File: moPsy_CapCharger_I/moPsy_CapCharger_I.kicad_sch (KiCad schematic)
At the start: 11 parts, among them J1 Conn_01x08_Male, U1 LM79L12_TO92, U2 LM555xN

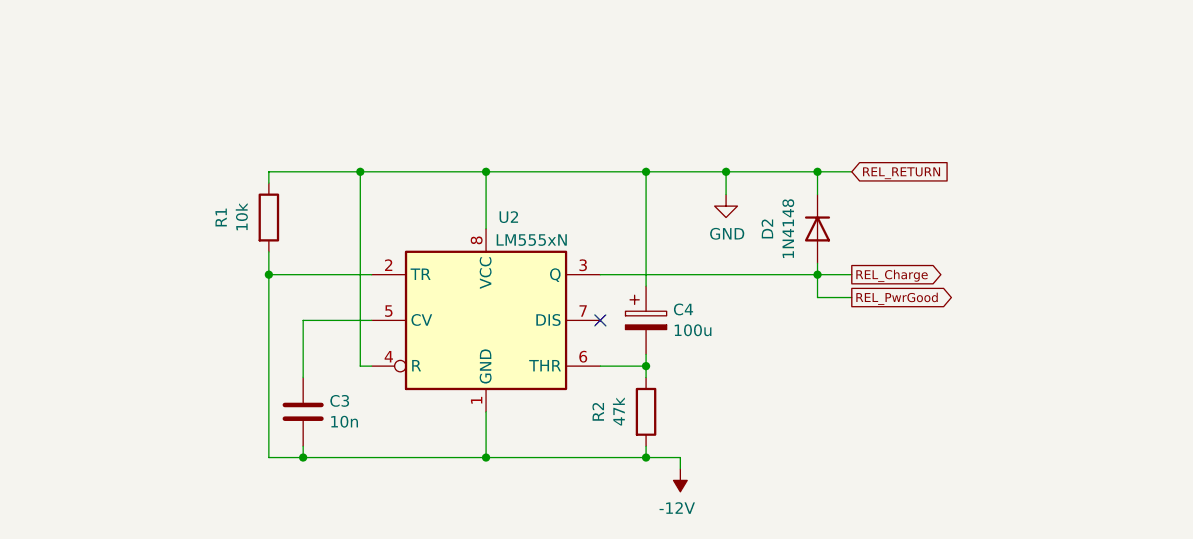
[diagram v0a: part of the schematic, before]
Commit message: Fix the Cap Charger circuit
The previous circuit did the wrong thing. This one is based
on https://elektro.turanis.de/html/prj248/index.html and has
the correct behaviour.

In the end, an RC element and a trigger are needed.
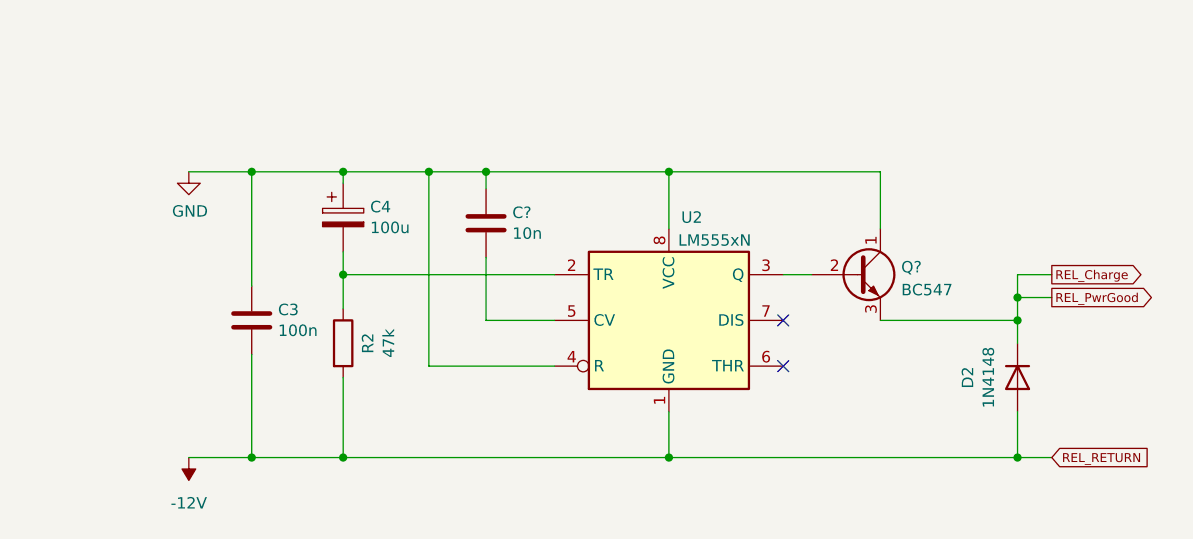
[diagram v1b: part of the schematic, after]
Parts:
- removed R1: 10k, Resistor_THT:R_Axial_DIN0207_L6.3mm_D2.5mm_P7.62mm_Horizontal, symbol Device:R
- added C?: 10n, Capacitor_THT:C_Rect_L7.0mm_W2.5mm_P5.00mm, symbol Device:C
- added Q?: BC547, Package_TO_SOT_THT:TO-92_Inline, symbol Transistor_BJT:BC547
- C2: footprint Capacitor_THT:CP_Radial_D8.0mm_P3.50mm -> Capacitor_THT:C_Rect_L7.0mm_W2.5mm_P5.00mm
- C3: value 10n -> 100n
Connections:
- net -12V: now also D2.2 (A), J1.8 (Pin_8); no longer U2.2 (TR)
- net GND: now also C3.1, C?.1, Q?.1 (C); no longer D2.1 (K), J1.8 (Pin_8)
- net REL_Charge: now also D2.1 (K), Q?.3 (E); no longer D2.2 (A), U2.3 (Q)
- net at U2.5 (CV): now also C?.2; no longer C3.1
- net at C4.2, R2.1: now also U2.2 (TR); no longer U2.6 (THR)
- new net: Q?.2 (B), U2.3 (Q)
- no-connect marks 1 -> 2
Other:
- moved on the sheet: C3, C4, D2, R2, U2

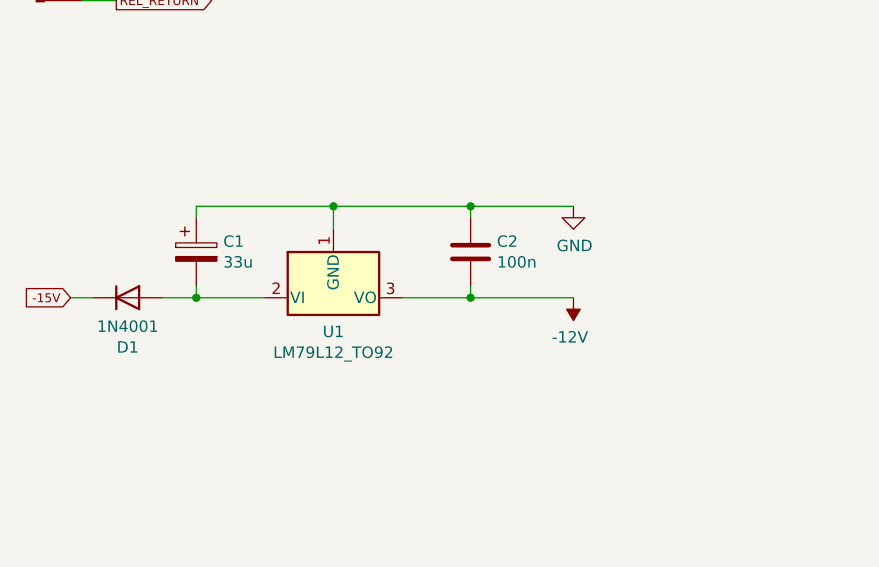
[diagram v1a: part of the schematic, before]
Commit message: Add a charge capacitor
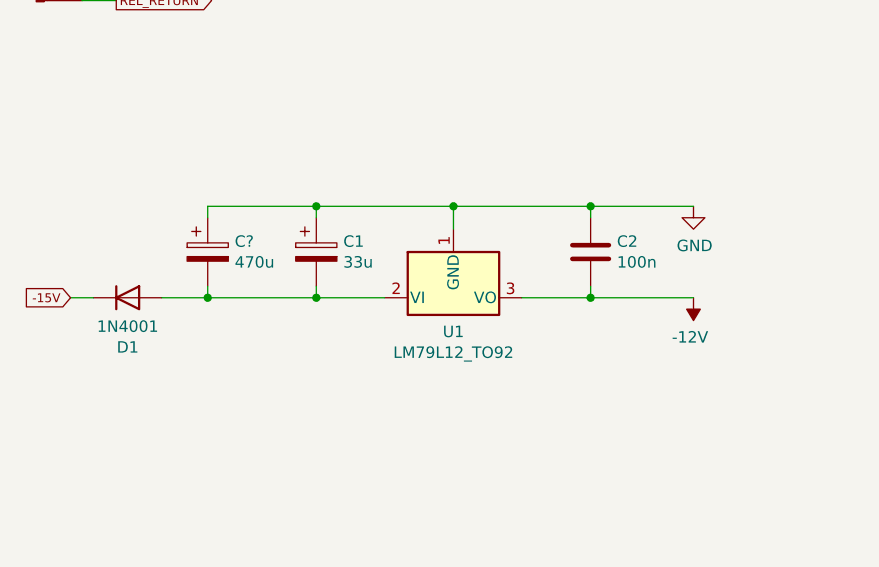
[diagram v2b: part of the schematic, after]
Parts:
- added C?: 470u, Capacitor_THT:CP_Radial_D8.0mm_P3.50mm, symbol Device:CP
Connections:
- net GND: now also C?.1
- net at C1.2, D1.2 (A), U1.2 (VI): now also C?.2
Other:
- moved on the sheet: C1, C2, U1

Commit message: Design a new PCB for the cap charger
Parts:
- C1: renamed from C?; footprint Capacitor_THT:CP_Radial_D8.0mm_P3.50mm -> Capacitor_THT:C_Axial_L19.0mm_D9.5mm_P25.00mm_Horizontal
- C4: renamed from C3; Reichelt (none) -> COS 105 470/16
- gave numbers to parts that had none: 2
- renumbered C1 to C2, C2 to C3, C4 to C5, R2 to R1
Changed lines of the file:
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@@
   (symbol (lib_id "Device:CP") (at 52.705 67.31 0) (unit 1)
     (in_bom yes) (on_board yes)
-    (property "Reference" "C1" (id 0) (at 55.7022 66.1416 0)
+    (property "Reference" "C2" (id 0) (at 55.7022 66.1416 0)
       (effects (font (size 1.27 1.27)) (justify left))
     )
@@
   (symbol (lib_id "Device:C") (at 83.185 67.31 0) (unit 1)
     (in_bom yes) (on_board yes)
-    (property "Reference" "C2" (id 0) (at 86.106 66.1416 0)
+    (property "Reference" "C3" (id 0) (at 86.106 66.1416 0)
       (effects (font (size 1.27 1.27)) (justify left))
     )
@@
   (symbol (lib_id "power:-12V") (at 94.615 72.39 180) (unit 1)
     (in_bom yes) (on_board yes)
-    (property "Reference" "#PWR0104" (id 0) (at 94.615 74.93 0)
+    (property "Reference" "#PWR03" (id 0) (at 94.615 74.93 0)
       (effects (font (size 1.27 1.27)) hide)
     )
@@
   (symbol (lib_id "power:GND") (at 94.615 62.23 0) (unit 1)
     (in_bom yes) (on_board yes)
-    (property "Reference" "#PWR0103" (id 0) (at 94.615 68.58 0)
+    (property "Reference" "#PWR02" (id 0) (at 94.615 68.58 0)
       (effects (font (size 1.27 1.27)) hide)
     )
@@
   (symbol (lib_id "Device:CP") (at 141.605 81.28 0) (unit 1)
     (in_bom yes) (on_board yes)
-    (property "Reference" "C4" (id 0) (at 144.6022 80.1116 0)
+    (property "Reference" "C5" (id 0) (at 144.6022 80.1116 0)
       (effects (font (size 1.27 1.27)) (justify left))
     )
@@
   (symbol (lib_id "Device:R") (at 141.605 95.25 0) (unit 1)
     (in_bom yes) (on_board yes)
-    (property "Reference" "R2" (id 0) (at 144.3736 95.25 90))
+    (property "Reference" "R1" (id 0) (at 144.3736 95.25 90))
     (property "Value" "47k" (id 1) (at 146.685 95.25 90))
     (property "Footprint" "Resistor_THT:R_Axial_DIN0207_L6.3mm_D2.5mm_P7.62mm_Horizontal" (id 2) (at 139.827 95.25 90)
@@
   (symbol (lib_id "power:-12V") (at 124.46 107.95 180) (unit 1)
     (in_bom yes) (on_board yes)
-    (property "Reference" "#PWR0101" (id 0) (at 124.46 110.49 0)
+    (property "Reference" "#PWR05" (id 0) (at 124.46 110.49 0)
       (effects (font (size 1.27 1.27)) hide)
     )
@@
   (symbol (lib_id "power:GND") (at 124.46 76.2 0) (unit 1)
     (in_bom yes) (on_board yes)
-    (property "Reference" "#PWR0102" (id 0) (at 124.46 82.55 0)
+    (property "Reference" "#PWR04" (id 0) (at 124.46 82.55 0)
       (effects (font (size 1.27 1.27)) hide)
     )
@@
   (symbol (lib_id "Device:C") (at 131.445 92.71 0) (unit 1)
     (in_bom yes) (on_board yes)
-    (property "Reference" "C3" (id 0) (at 134.366 91.5416 0)
+    (property "Reference" "C4" (id 0) (at 134.366 91.5416 0)
       (effects (font (size 1.27 1.27)) (justify left))
     )
@@
     )
     (property "Datasheet" "~" (id 3) (at 131.445 92.71 0)
+      (effects (font (size 1.27 1.27)) hide)
+    )
+    (property "Reichelt" "COS 105 470/16" (id 4) (at 131.445 92.71 0)
       (effects (font (size 1.27 1.27)) hide)
     )
@@
   (symbol (lib_id "power:GND") (at 44.45 25.4 0) (unit 1)
     (in_bom yes) (on_board yes)
-    (property "Reference" "#PWR0105" (id 0) (at 44.45 31.75 0)
+    (property "Reference" "#PWR01" (id 0) (at 44.45 31.75 0)
       (effects (font (size 1.27 1.27)) hide)
     )
@@
   (symbol (lib_id "Device:CP") (at 40.64 67.31 0) (unit 1)
     (in_bom yes) (on_board yes)
-    (property "Reference" "C?" (id 0) (at 43.6372 66.1416 0)
+    (property "Reference" "C1" (id 0) (at 43.6372 66.1416 0)
       (effects (font (size 1.27 1.27)) (justify left))
     )
@@
       (effects (font (size 1.27 1.27)) (justify left))
     )
-    (property "Footprint" "Capacitor_THT:CP_Radial_D8.0mm_P3.50mm" (id 2) (at 41.6052 71.12 0)
+    (property "Footprint" "Capacitor_THT:C_Axial_L19.0mm_D9.5mm_P25.00mm_Horizontal" (id 2) (at 41.6052 71.12 0)
       (effects (font (size 1.27 1.27)) hide)
     )
@@
   (symbol (lib_id "Transistor_BJT:BC547") (at 198.755 87.63 0) (unit 1)
     (in_bom yes) (on_board yes) (fields_autoplaced)
-    (property "Reference" "Q?" (id 0) (at 203.6064 86.7953 0)
+    (property "Reference" "Q1" (id 0) (at 203.6064 86.7953 0)
       (effects (font (size 1.27 1.27)) (justify left))
     )
@@
   (symbol (lib_id "Device:C") (at 157.48 81.915 0) (unit 1)
     (in_bom yes) (on_board yes)
-    (property "Reference" "C?" (id 0) (at 160.401 80.7466 0)
+    (property "Reference" "C6" (id 0) (at 160.401 80.7466 0)
       (effects (font (size 1.27 1.27)) (justify left))
     )
@@
   )
   (symbol_instances
+    (path "/00000000-0000-0000-0000-0000613c2ab8"
+      (reference "#PWR01") (unit 1) (value "GND") (footprint "")
+    )
+    (path "/00000000-0000-0000-0000-0000612b1793"
+      (reference "#PWR02") (unit 1) (value "GND") (footprint "")
+    )
+    (path "/00000000-0000-0000-0000-0000612a8ee9"
+      (reference "#PWR03") (unit 1) (value "-12V") (footprint "")
+    )
+    (path "/00000000-0000-0000-0000-00006130a3f6"
+      (reference "#PWR04") (unit 1) (value "GND") (footprint "")
+    )
     (path "/00000000-0000-0000-0000-0000612ff71a"
-      (reference "#PWR0101") (unit 1) (value "-12V") (footprint "")
-    )
-    (path "/00000000-0000-0000-0000-00006130a3f6"
-      (reference "#PWR0102") (unit 1) (value "GND") (footprint "")
-    )
-    (path "/00000000-0000-0000-0000-0000612b1793"
-      (reference "#PWR0103") (unit 1) (value "GND") (footprint "")
-    )
-    (path "/00000000-0000-0000-0000-0000612a8ee9"
-      (reference "#PWR0104") (unit 1) (value "-12V") (footprint "")
-    )
-    (path "/00000000-0000-0000-0000-0000613c2ab8"
-      (reference "#PWR0105") (unit 1) (value "GND") (footprint "")
+      (reference "#PWR05") (unit 1) (value "-12V") (footprint "")
+    )
+    (path "/078f9a7f-ac2c-4d40-9222-e8150d7dd944"
+      (reference "C1") (unit 1) (value "470u") (footprint "Capacitor_THT:C_Axial_L19.0mm_D9.5mm_P25.00mm_Horizontal")
     )
     (path "/00000000-0000-0000-0000-000061297317"
-      (reference "C1") (unit 1) (value "33u") (footprint "Capacitor_THT:CP_Radial_D8.0mm_P3.50mm")
+      (reference "C2") (unit 1) (value "33u") (footprint "Capacitor_THT:CP_Radial_D8.0mm_P3.50mm")
     )
     (path "/00000000-0000-0000-0000-000061297bec"
-      (reference "C2") (unit 1) (value "100n") (footprint "Capacitor_THT:C_Rect_L7.0mm_W2.5mm_P5.00mm")
+      (reference "C3") (unit 1) (value "100n") (footprint "Capacitor_THT:C_Rect_L7.0mm_W2.5mm_P5.00mm")
     )
     (path "/00000000-0000-0000-0000-000061397e46"
-      (reference "C3") (unit 1) (value "100n") (footprint "Capacitor_THT:C_Rect_L7.0mm_W2.5mm_P5.00mm")
+      (reference "C4") (unit 1) (value "100n") (footprint "Capacitor_THT:C_Rect_L7.0mm_W2.5mm_P5.00mm")
     )
     (path "/00000000-0000-0000-0000-0000612e7d4e"
-      (reference "C4") (unit 1) (value "100u") (footprint "Capacitor_THT:CP_Radial_D8.0mm_P3.50mm")
-    )
-    (path "/078f9a7f-ac2c-4d40-9222-e8150d7dd944"
-      (reference "C?") (unit 1) (value "470u") (footprint "Capacitor_THT:CP_Radial_D8.0mm_P3.50mm")
+      (reference "C5") (unit 1) (value "100u") (footprint "Capacitor_THT:CP_Radial_D8.0mm_P3.50mm")
     )
     (path "/f78b27e0-23ca-4f72-96a5-deeb73caf462"
-      (reference "C?") (unit 1) (value "10n") (footprint "Capacitor_THT:C_Rect_L7.0mm_W2.5mm_P5.00mm")
+      (reference "C6") (unit 1) (value "10n") (footprint "Capacitor_THT:C_Rect_L7.0mm_W2.5mm_P5.00mm")
     )
     (path "/00000000-0000-0000-0000-00006143c414"
@@
     )
     (path "/9d5795a6-ff04-4973-86db-499f30805dd6"
-      (reference "Q?") (unit 1) (value "BC547") (footprint "Package_TO_SOT_THT:TO-92_Inline")
+      (reference "Q1") (unit 1) (value "BC547") (footprint "Package_TO_SOT_THT:TO-92_Inline")
     )
     (path "/00000000-0000-0000-0000-0000612e851c"
-      (reference "R2") (unit 1) (value "47k") (footprint "Resistor_THT:R_Axial_DIN0207_L6.3mm_D2.5mm_P7.62mm_Horizontal")
+      (reference "R1") (unit 1) (value "47k") (footprint "Resistor_THT:R_Axial_DIN0207_L6.3mm_D2.5mm_P7.62mm_Horizontal")
     )
     (path "/00000000-0000-0000-0000-000061295ff0"

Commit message: Add fix for delay circuit
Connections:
- net at C5.2, R1.1, U2.2 (TR): now also U2.6 (THR)
- no-connect marks 2 -> 1
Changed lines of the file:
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@@
   (junction (at 131.445 107.95) (diameter 0) (color 0 0 0 0)
   )
+  (junction (at 163.83 87.63) (diameter 0) (color 0 0 0 0)
+  )
   (junction (at 141.605 87.63) (diameter 0) (color 0 0 0 0)
   )
@@
   )
   (no_connect (at 190.5 92.71))
-  (no_connect (at 190.5 97.79))
   (wire (pts (xy 201.295 92.71) (xy 216.535 92.71))
     (stroke (width 0) (type default) (color 0 0 0 0))
@@
     (stroke (width 0) (type default) (color 0 0 0 0))
   )
+  (wire (pts (xy 190.5 97.79) (xy 193.675 97.79))
+    (stroke (width 0) (type default) (color 0 0 0 0))
+  )
   (wire (pts (xy 131.445 107.95) (xy 141.605 107.95))
     (stroke (width 0) (type default) (color 0 0 0 0))
@@
     (stroke (width 0) (type default) (color 0 0 0 0))
   )
-  (wire (pts (xy 165.1 87.63) (xy 141.605 87.63))
+  (wire (pts (xy 165.1 87.63) (xy 163.83 87.63))
     (stroke (width 0) (type default) (color 0 0 0 0))
   )
@@
     (stroke (width 0) (type default) (color 0 0 0 0))
   )
+  (wire (pts (xy 193.675 104.14) (xy 163.83 104.14))
+    (stroke (width 0) (type default) (color 0 0 0 0))
+  )
   (wire (pts (xy 141.605 76.2) (xy 131.445 76.2))
     (stroke (width 0) (type default) (color 0 0 0 0))
@@
     (stroke (width 0) (type default) (color 0 0 0 0))
   )
+  (wire (pts (xy 163.83 104.14) (xy 163.83 87.63))
+    (stroke (width 0) (type default) (color 0 0 0 0))
+  )
   (wire (pts (xy 83.185 71.12) (xy 83.185 72.39))
     (stroke (width 0) (type default) (color 0 0 0 0))
@@
     (stroke (width 0) (type default) (color 0 0 0 0))
   )
+  (wire (pts (xy 163.83 87.63) (xy 141.605 87.63))
+    (stroke (width 0) (type default) (color 0 0 0 0))
+  )
   (wire (pts (xy 141.605 107.95) (xy 177.8 107.95))
     (stroke (width 0) (type default) (color 0 0 0 0))
@@
     (stroke (width 0) (type default) (color 0 0 0 0))
   )
+  (wire (pts (xy 193.675 97.79) (xy 193.675 104.14))
+    (stroke (width 0) (type default) (color 0 0 0 0))
+  )
